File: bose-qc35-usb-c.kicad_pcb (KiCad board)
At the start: 4 copper layers, 24 x 16 mm, 37 parts, among them J1 502426-2030, J2 TYPE-C-31-M-12, J3 51281-0594, Q1 BC846BM3T5G, U1 TPS25200

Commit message: Clarify component choices
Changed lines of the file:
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@@
-(kicad_pcb (version 20210925) (generator pcbnew)
+(kicad_pcb (version 20211014) (generator pcbnew)
   (general
     (thickness 1.6)
@@
     )
   )
-  (gr_arc (start 82.684195 82.216599) (end 86.040701 59.081934) (angle -61.79410705) (layer "Edge.Cuts") (width 0.000159))
-  (gr_arc (start 66.208024 73.856368) (end 65.878193 73.60021) (angle -118.2099629) (layer "Edge.Cuts") (width 0.000159))
-  (gr_arc (start 90.401727 92.649426) (end 81.000089 66.966304) (angle -29.3191517) (layer "Edge.Cuts") (width 0.000159))
+  (gr_arc (start 63.883083 68.324261) (mid 73.6848 60.641388) (end 86.040701 59.081934) (layer "Edge.Cuts") (width 0.000159))
+  (gr_arc (start 66.138205 74.268109) (mid 65.818855 74.007871) (end 65.878193 73.60021) (layer "Edge.Cuts") (width 0.000159))
+  (gr_arc (start 69.628031 74.859904) (mid 74.806378 70.181702) (end 81.000089 66.966304) (layer "Edge.Cuts") (width 0.000159))
   (gr_line (start 69.628033 74.859908) (end 66.138201 74.268109) (layer "Edge.Cuts") (width 0.000159))
   (gr_line (start 86.040701 59.081934) (end 85.983941 60.877098) (layer "Edge.Cuts") (width 0.000159))
-  (gr_arc (start 64.250421 72.33601) (end 65.878193 73.60021) (angle -73.83729161) (layer "Edge.Cuts") (width 0.000159))
+  (gr_arc (start 65.91777 71.124486) (mid 66.311187 72.368954) (end 65.878193 73.60021) (layer "Edge.Cuts") (width 0.000159))
   (gr_line (start 87.895775 64.442049) (end 81.000089 66.966304) (layer "Edge.Cuts") (width 0.000159))
   (gr_line (start 65.917772 71.124486) (end 63.883084 68.324265) (layer "Edge.Cuts") (width 0.000159))

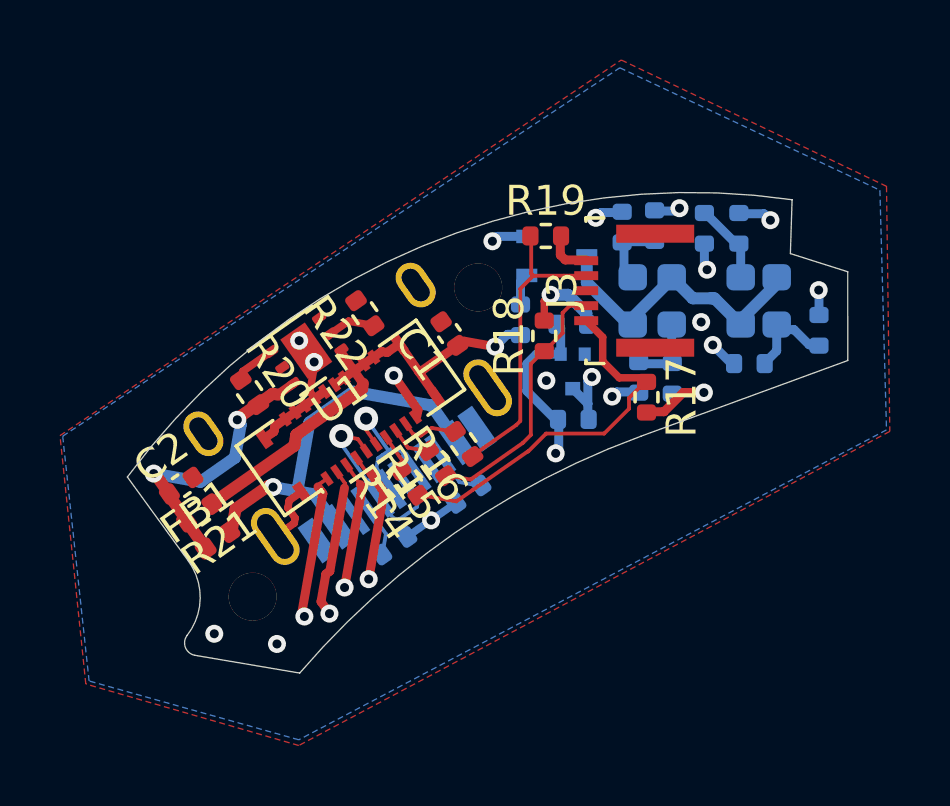
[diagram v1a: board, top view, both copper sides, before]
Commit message: Update shematic for calrity and to kicad 7
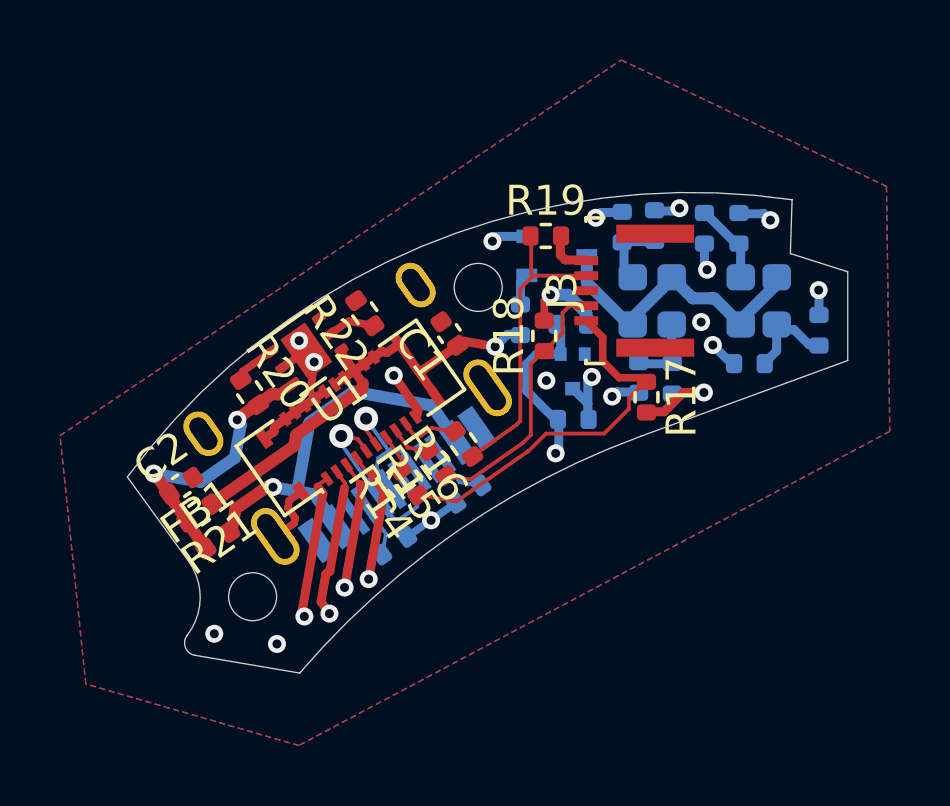
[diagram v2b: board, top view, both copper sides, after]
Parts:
- D1: value LED -> ORH-G36G
- D2: value LED -> ORH-R36G
- D3: value LED -> ORH-W46G
- D4: value LED -> ORH-B36G
- R1, R17, R18, R19, R2, R3, R4: value R -> CG0402MLC-05LG
- R21, R5: value *0R -> 0R
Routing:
- net GND: track 18.5 -> 19.5 mm

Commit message: Use alternative USB C port which doesn't require modification
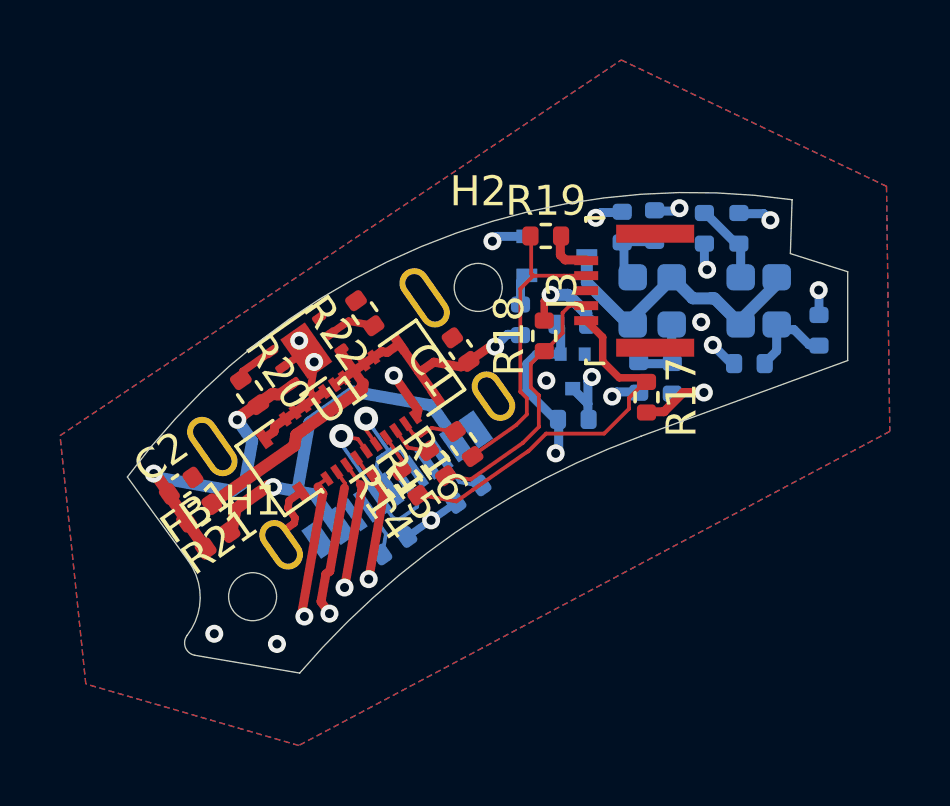
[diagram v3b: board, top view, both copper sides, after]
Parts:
- H1, H2: footprint MountingHole:MountingHole_2.1mm -> library:MountingHole_1.6mm
- J1: footprint Connector_Molex:Molex_SlimStack_502426-2010_2x10_P0.40mm_Vertical -> library:Molex_SlimStack_502426-2010_2x10_P0.40mm_Vertical
- J2: value TYPE-C-31-M-12 -> 2171790001; footprint Connector_USB:USB_C_Receptacle_HRO_TYPE-C-31-M-12 -> library:USB_C_Receptacle_Molex_2171790001
- J3: footprint Connector_FFC-FPC:TE_0-1734839-5_1x05-1MP_P0.5mm_Horizontal -> library:TE_0-1734839-5_1x05-1MP_P0.5mm_Horizontal
- U1: footprint Package_SON:WSON-6-1EP_2x2mm_P0.65mm_EP1x1.6mm -> library:WSON-6-1EP_2x2mm_P0.65mm_EP1x1.6mm
- moved C1 0.65 mm to (75.0, 64.1)
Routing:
- net +5V: track 9.68 -> 10.9 mm

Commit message: Update Molex connector model
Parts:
- J3: value 51281-0594 -> 51281-0598
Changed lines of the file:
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@@
         (effects (font (size 1 1) (thickness 0.15)))
     )
-    (fp_text value "51281-0594" (at 0 2.05 90) (layer "Dwgs.User")
+    (fp_text value "51281-0598" (at 0 2.05 90) (layer "Dwgs.User")
         (effects (font (size 0.5 0.5) (thickness 0.08)))
     )
